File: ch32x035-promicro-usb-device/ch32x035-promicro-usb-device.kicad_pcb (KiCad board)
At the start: 2 copper layers, 17.8 x 31.8 mm, 26 parts, among them J1 USB_TypeC-2.0_Receptacle, J2 SWD_10Pin_MCU-Side, SW1 SW_Push, U1 AMS1117-3.3, U2 CH32X035G8U6, U3 CH217K

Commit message: ch32x035-usb-device
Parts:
- J1: value USB_TypeC-2.0_Receptacle -> 217179-0001
- SW1: value SW_Push -> RESET
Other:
- board text added: "USB-DEV"
- board text removed: "ProMicro"

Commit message: ch32x035-usb-device
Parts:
- added REF**: JLCJLCJLCJLC, 74th:Logo_JLCJLCJLCJLC, B.Cu at (75.0, 64.9)
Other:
- board text added: "DCK"
- board text added: "DIO"
- board text removed: "SWCL"
- board text removed: "SWDIO"
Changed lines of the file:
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@@
     (fp_line (start 1 0.6) (end 1 -0.6)
       (stroke (width 0.1) (type solid)) (layer "F.Fab"))
-    (pad "1" smd roundrect (at -1.025 0 90) (size 1.15 1.4) (layers "F.Cu" "F.Paste" "F.Mask") (roundrect_rratio 0.217391)
+    (pad "1" smd roundrect (at -1.025 0 90) (size 1.15 1.4) (layers "F.Cu" "F.Paste" "F.Mask") (roundrect_rratio 0.2173913043)
       (net 27 "GND") (pinfunction "K") (pintype "passive"))
-    (pad "2" smd roundrect (at 1.025 0 90) (size 1.15 1.4) (layers "F.Cu" "F.Paste" "F.Mask") (roundrect_rratio 0.217391)
+    (pad "2" smd roundrect (at 1.025 0 90) (size 1.15 1.4) (layers "F.Cu" "F.Paste" "F.Mask") (roundrect_rratio 0.2173913043)
       (net 16 "Net-(D1-A)") (pinfunction "A") (pintype "passive"))
     (model "${KICAD6_3DMODEL_DIR}/LED_SMD.3dshapes/LED_0805_2012Metric.wrl"
@@
       (scale (xyz 1 1 1))
       (rotate (xyz 0 0 0))
+    )
+  )
+  (footprint "74th:Logo_JLCJLCJLCJLC" (layer "B.Cu")
+    (at 75.05 64.9 90)
+    (attr smd)
+    (fp_text reference "REF**" (at 0 1.6 270 unlocked) (layer "B.SilkS") hide
+        (effects (font (size 1 1) (thickness 0.15)) (justify mirror))
+    )
+    (fp_text value "JLCJLCJLCJLC" (at 0 0 270 unlocked) (layer "B.SilkS")
+        (effects (font (size 0.8 0.8) (thickness 0.15)) (justify mirror))
     )
   )
@@
     (effects (font (size 0.8 0.8) (thickness 0.12)) (justify right bottom))
   )
-  (gr_text "SWCL" (at 74.45 68.25 45) (layer "F.SilkS")
+  (gr_text "DCK" (at 74.45 68.25 45) (layer "F.SilkS")
     (effects (font (size 0.8 0.8) (thickness 0.12)) (justify left bottom))
   )
@@
     (effects (font (size 0.8 0.8) (thickness 0.12)) (justify right bottom))
   )
-  (gr_text "SWDIO" (at 74.3 65.55 45) (layer "F.SilkS")
+  (gr_text "DIO" (at 74.3 65.55 45) (layer "F.SilkS")
     (effects (font (size 0.8 0.8) (thickness 0.12)) (justify left bottom))
   )

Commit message: ch32x035
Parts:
- SW1: value RESET -> SKRPABE010
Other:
- board text added: "C18"
- board text added: "C19"
- board text removed: "A18"
- board text removed: "A19"
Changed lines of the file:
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@@
         (effects (font (size 0.8 0.8) (thickness 0.12)))
     )
-    (fp_text value "RESET" (at -0.2156 -1.8938 unlocked) (layer "F.SilkS")
+    (fp_text value "SKRPABE010" (at -0.2156 -1.8938 unlocked) (layer "F.SilkS")
         (effects (font (size 0.8 0.8) (thickness 0.12)))
     )
@@
     (effects (font (size 0.8 0.8) (thickness 0.12)) (justify left bottom))
   )
-  (gr_text "A18" (at 74.95 69.15 45) (layer "F.SilkS")
+  (gr_text "C18" (at 74.95 69.15 45) (layer "F.SilkS")
     (effects (font (size 0.8 0.8) (thickness 0.12)) (justify left bottom))
   )
@@
     (effects (font (size 0.8 0.8) (thickness 0.12)) (justify left bottom))
   )
-  (gr_text "A19" (at 74.95 66.4 45) (layer "F.SilkS")
+  (gr_text "C19" (at 74.95 66.4 45) (layer "F.SilkS")
     (effects (font (size 0.8 0.8) (thickness 0.12)) (justify left bottom))
   )

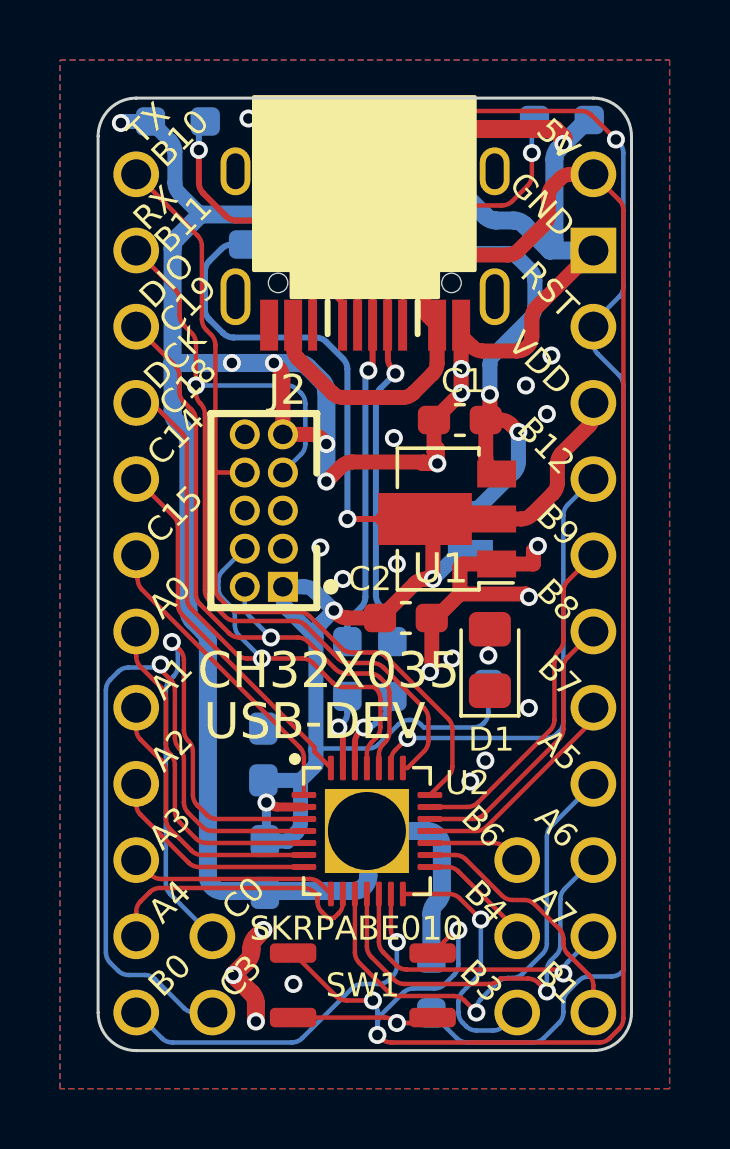
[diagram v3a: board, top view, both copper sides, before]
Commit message: fix SWDIO/SWCLK
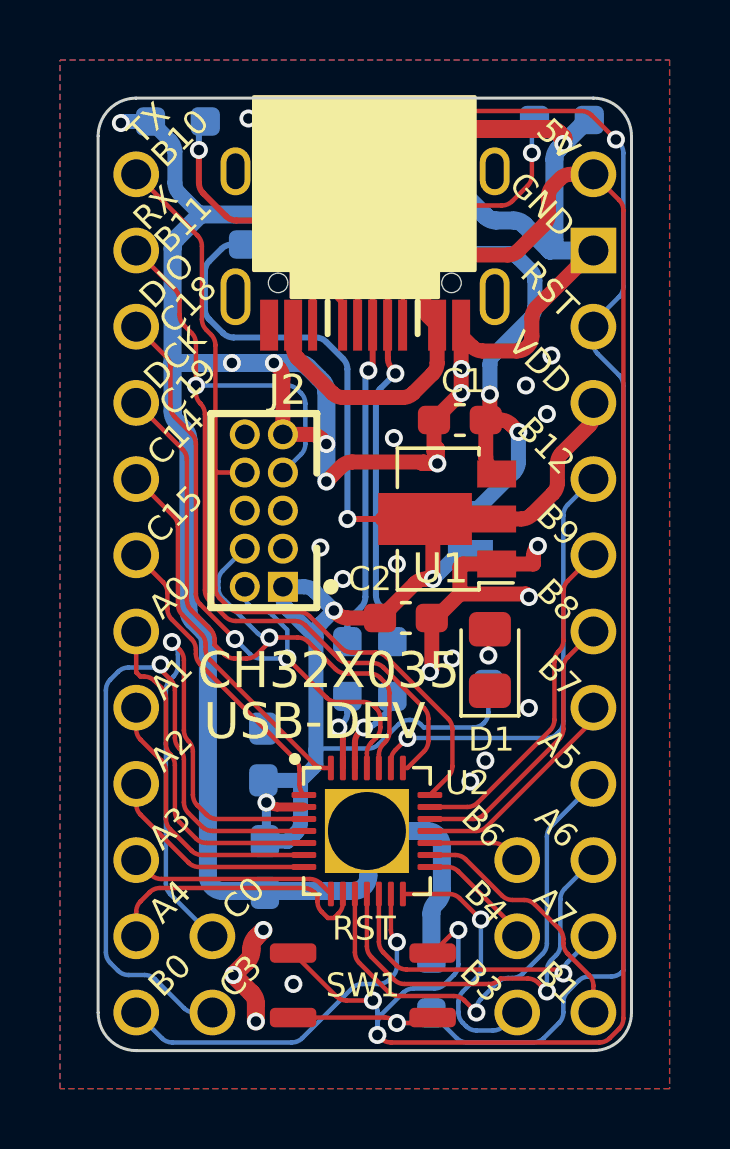
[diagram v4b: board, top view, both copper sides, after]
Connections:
- U2 pad 24: /SWDIO -> /SWCLK
- U2 pad 25: /SWCLK -> /SWDIO
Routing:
- net /SWCLK: track 21.9 -> 23.7 mm
- net /SWDIO: track 22.2 -> 22.6 mm, vias 1 -> 2
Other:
- board text added: "v1.0.1"
- board text removed: "v1.0.0"
